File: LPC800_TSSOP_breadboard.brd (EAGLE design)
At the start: 31.1 x 15.9 mm, 16 parts, among them Q1 12MHz

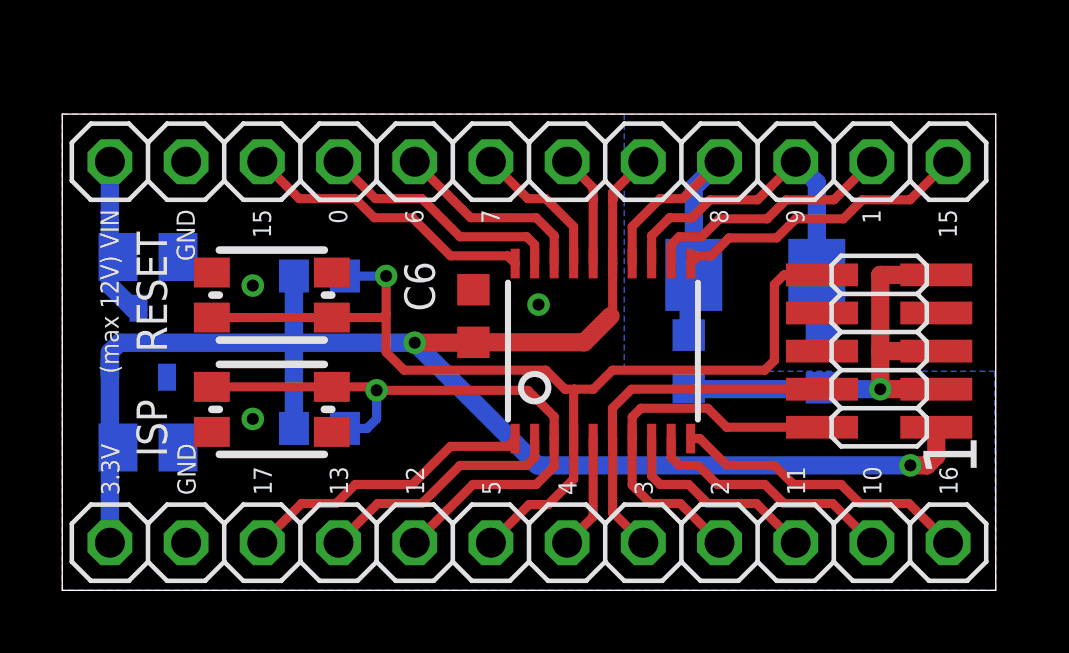
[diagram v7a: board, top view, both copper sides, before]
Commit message: * updated boards with cheaper buttons, better layout and indexed JTAG header
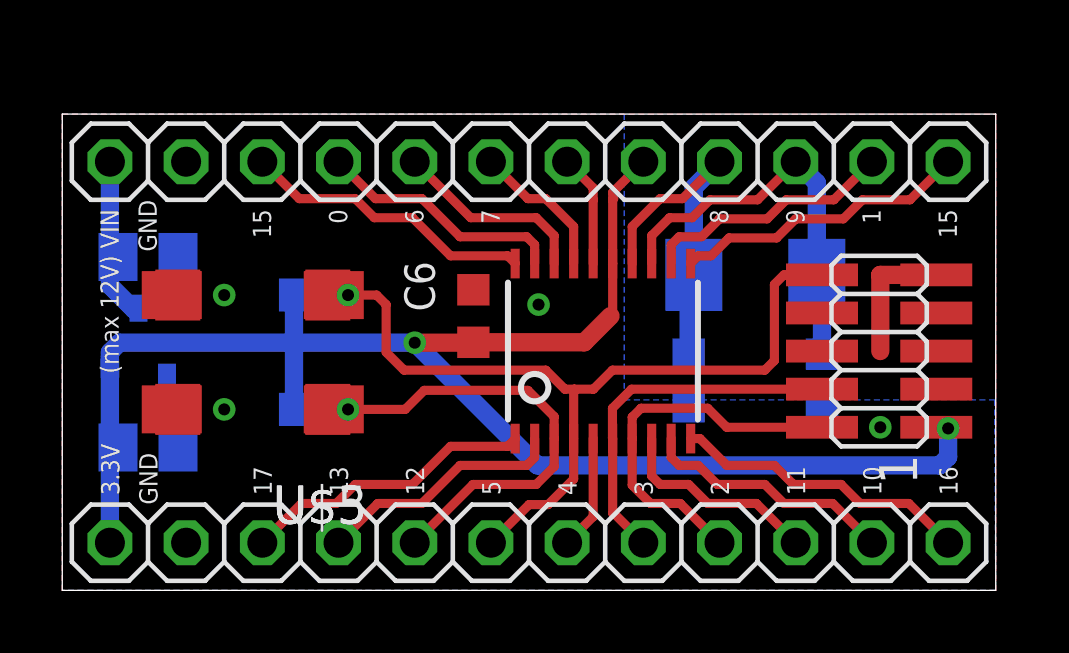
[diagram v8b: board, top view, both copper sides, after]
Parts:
- added U$1: TACT_2PINDTSM3, SquantorButtons:DTSM3
- added U$5: TACT_2PIN, SquantorButtons:TD-85XU
- JP3: device bart_connectors:2X05_1.27_SMD -> SquantorConnectors:2X05_1.27_SMD
- U$3: value RESET -> TACT_2PINDTSM3; device SquantorButtons:KMR2 -> SquantorButtons:DTSM3
- U$4: value ISP -> TACT_2PIN; device SquantorButtons:KMR2 -> SquantorButtons:TD-85XU
- moved U$3 3.86 mm to (6.35, 6.03), turned to 180 degrees
- moved U$4 3.86 mm to (6.35, 9.84), turned to 180 degrees
- moved C2 0.63 mm to (20.9, 7.00)
- moved C3 0.63 mm to (25.3, 7.00)
- moved R1 0.63 mm to (8.57, 6.03)
- moved R2 0.63 mm to (8.57, 9.84)
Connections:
- net PIO0_12: now also U$3.P$1, U$5.P$1; no longer U$4.1, U$4.2
- net PIO0_5: now also U$1.P$1, U$4.P$1; no longer U$3.1, U$3.2
- net VSS: now also U$1.P$2, U$3.P$2, U$4.P$2, U$5.P$2; no longer U$3.3, U$3.4, U$4.3, U$4.4
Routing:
- net VSS: track 19.6 -> 8.21 mm
- net PIO0_5: track 34.9 -> 28.5 mm
- net PIO0_12: track 21.3 -> 15.6 mm
- net PIO0_9: track 13.8 -> 14.4 mm
- net PIO0_8: track 12.1 -> 12.8 mm
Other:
- board text added: "V2014.10.08"
- board text removed: "V2014.05.29"
